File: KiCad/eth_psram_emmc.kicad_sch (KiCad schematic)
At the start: 42 parts, among them IC6 LAN8742A-CZ-TR, IC7 APS256XXN-OBR-BG, X2 5033981892, Y2 VXM7-9032-25M0000000

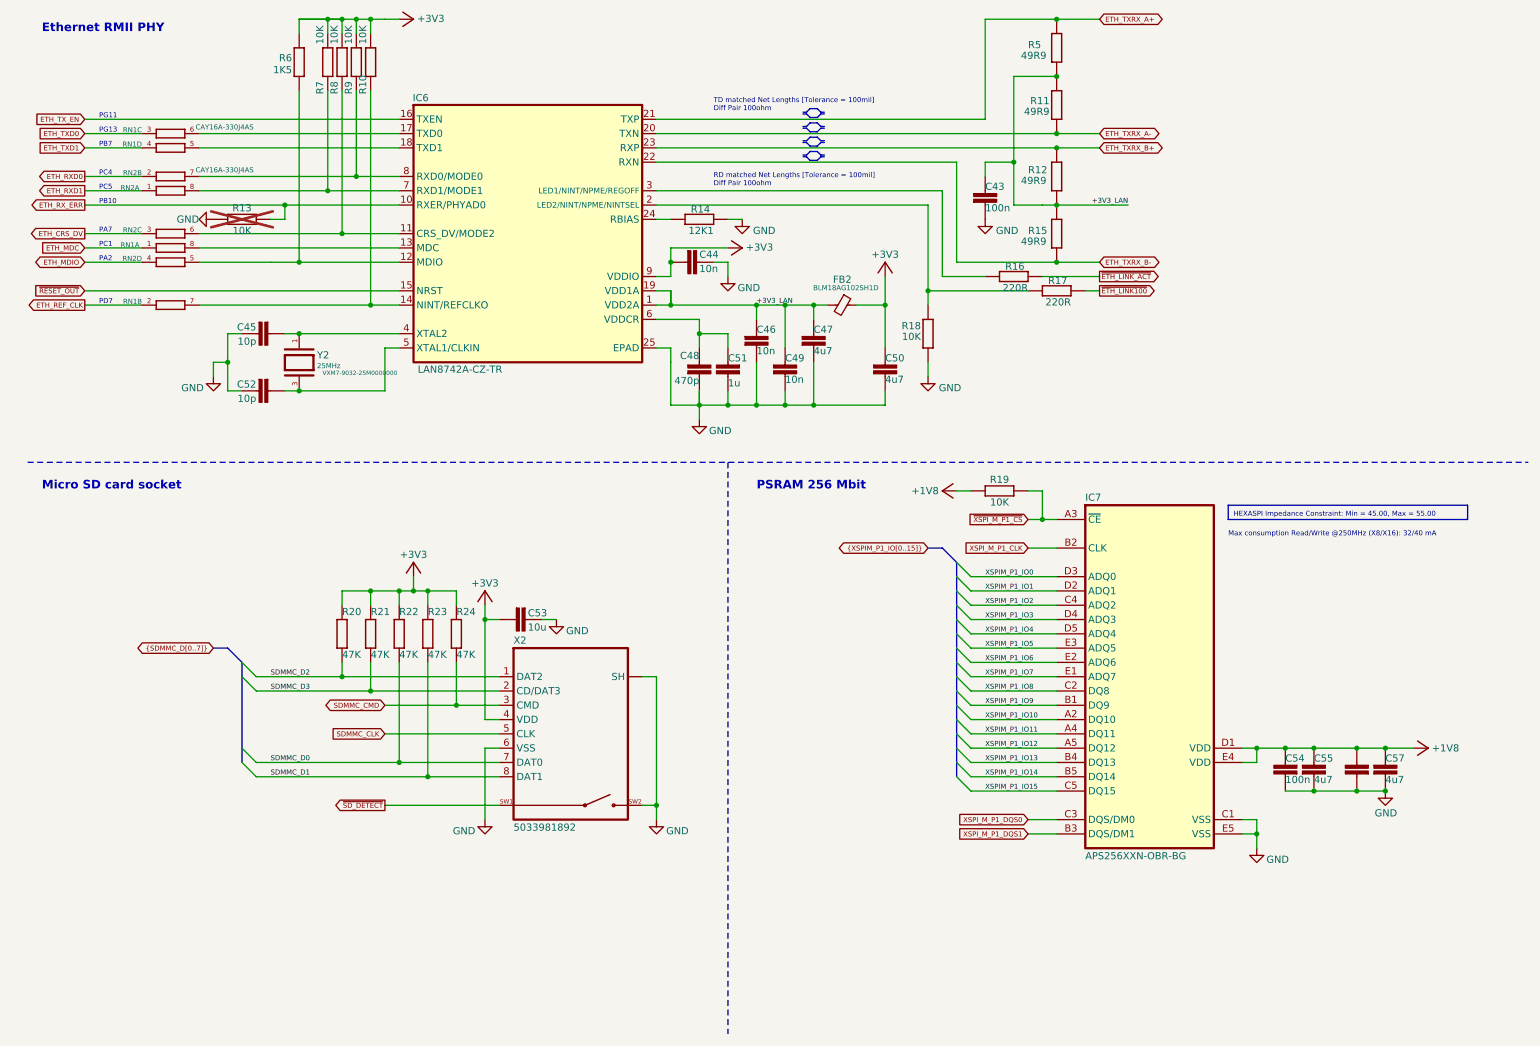
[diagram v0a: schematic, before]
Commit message: Split SoM footprint into two separate 100-pin connectors
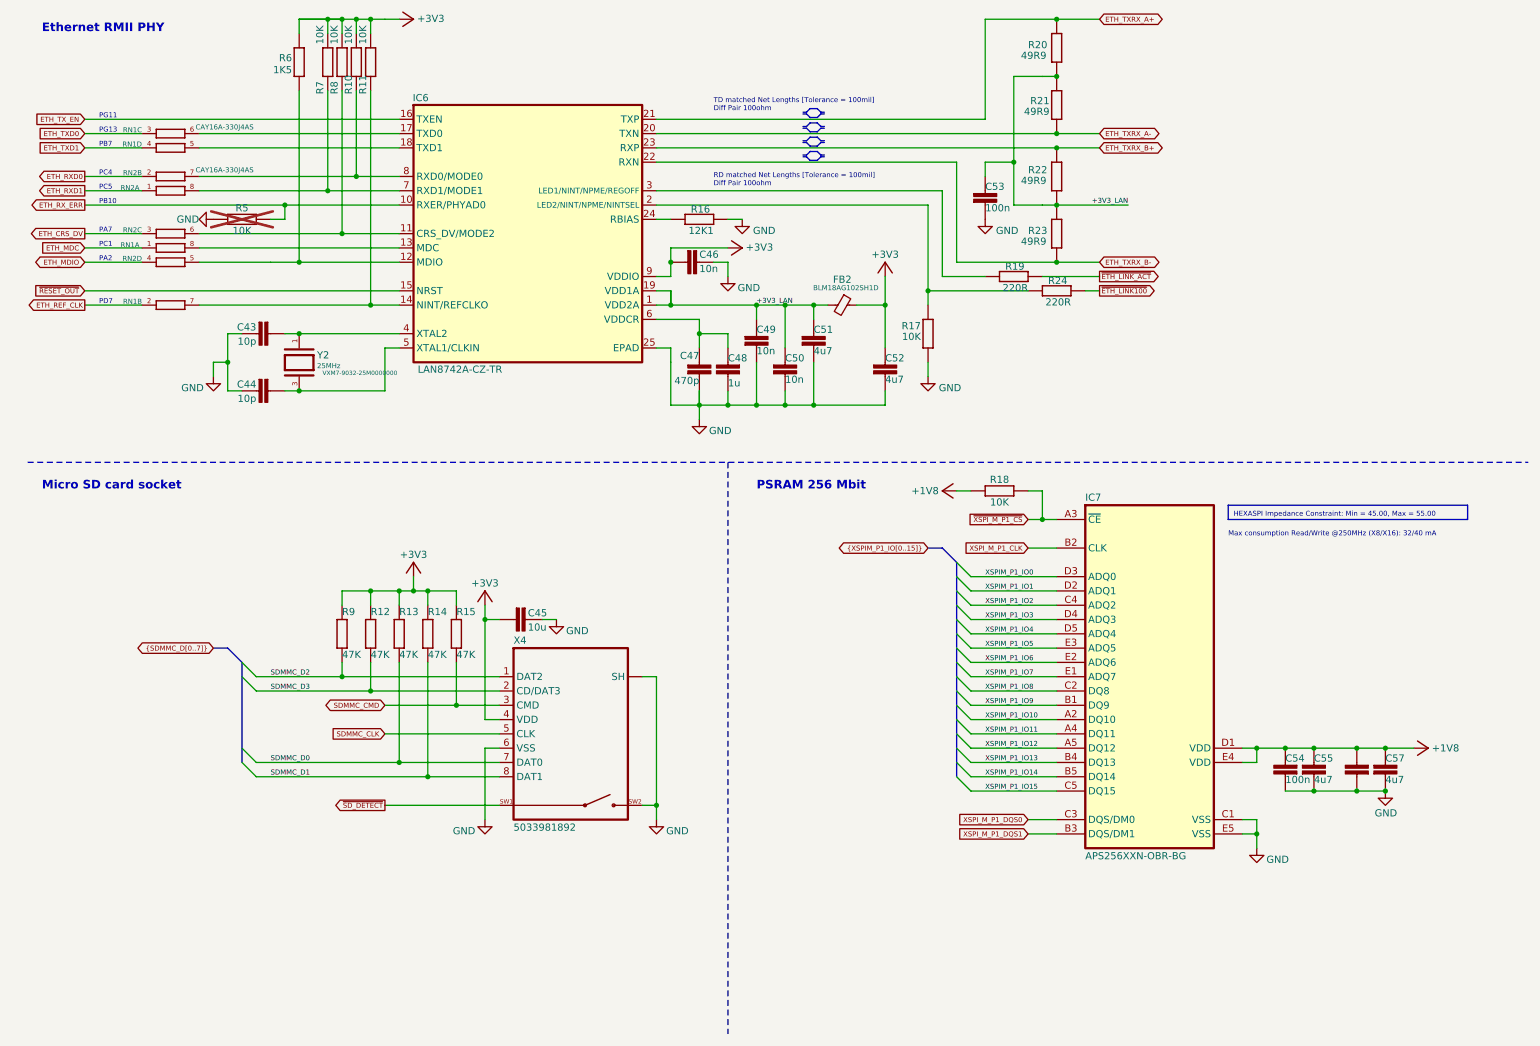
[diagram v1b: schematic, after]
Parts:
- renumbered C45 to C43, C52 to C44, C53 to C45, C44 to C46, C48 to C47, C51 to C48, C46 to C49, C49 to C50, C47 to C51, C50 to C52, C43 to C53, R9 to R10, R10 to R11, R21 to R12, R22 to R13, R23 to R14, R24 to R15, R14 to R16, R18 to R17, R19 to R18, R16 to R19, R5 to R20, R11 to R21, R12 to R22, R15 to R23, R17 to R24, R13 to R5, R20 to R9, X2 to X4

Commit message: #20
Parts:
- renumbered R9 to R10, R10 to R11, R11 to R12, R12 to R13, R13 to R14, R14 to R15, R15 to R16, R16 to R17, R17 to R18, R18 to R19, R19 to R20, R20 to R21, R21 to R22, R22 to R23, R23 to R24, R24 to R25, R5 to R6, R6 to R7, R7 to R8, R8 to R9
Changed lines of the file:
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@@
 	(title_block
 		(title "${project_name}")
-		(date "2026-04-18")
+		(date "2026-04-20")
 		(rev "${project_version}")
 		(company "${project_creator}")
@@
 		(in_pos_files yes)
 		(dnp no)
-		(property "Reference" "#+3V010"
+		(property "Reference" "#+3V011"
 			(at 83.82 15.24 0)
 			(hide yes)
@@
 			(project "BB3plus CM5 STM32H7 module"
 				(path "/1a4f0aea-3a69-423f-8790-3103cd0321c4/db533ab3-e8cc-4dba-934e-bd27ee1dfc29"
-					(reference "#+3V010")
+					(reference "#+3V011")
 					(unit 1)
 				)
@@
 		(in_pos_files yes)
 		(dnp no)
-		(property "Reference" "R16"
+		(property "Reference" "R17"
 			(at 136.525 48.26 90)
 			(show_name no)
@@
 			(project "BB3plus CM5 STM32H7 module"
 				(path "/1a4f0aea-3a69-423f-8790-3103cd0321c4/db533ab3-e8cc-4dba-934e-bd27ee1dfc29"
-					(reference "R16")
+					(reference "R17")
 					(unit 1)
 				)
@@
 		(in_pos_files yes)
 		(dnp no)
-		(property "Reference" "R7"
+		(property "Reference" "R8"
 			(at 67.945 28.575 90)
 			(show_name no)
@@
 			(project "BB3plus CM5 STM32H7 module"
 				(path "/1a4f0aea-3a69-423f-8790-3103cd0321c4/db533ab3-e8cc-4dba-934e-bd27ee1dfc29"
-					(reference "R7")
+					(reference "R8")
 					(unit 1)
 				)
@@
 		(in_pos_files yes)
 		(dnp no)
-		(property "Reference" "R14"
+		(property "Reference" "R15"
 			(at 86.36 121.285 0)
 			(show_name no)
@@
 			(project "BB3plus CM5 STM32H7 module"
 				(path "/1a4f0aea-3a69-423f-8790-3103cd0321c4/db533ab3-e8cc-4dba-934e-bd27ee1dfc29"
-					(reference "R14")
+					(reference "R15")
 					(unit 1)
 				)
@@
 		(in_pos_files yes)
 		(dnp no)
-		(property "Reference" "R9"
+		(property "Reference" "R10"
 			(at 71.12 121.285 0)
 			(show_name no)
@@
 			(project "BB3plus CM5 STM32H7 module"
 				(path "/1a4f0aea-3a69-423f-8790-3103cd0321c4/db533ab3-e8cc-4dba-934e-bd27ee1dfc29"
-					(reference "R9")
+					(reference "R10")
 					(unit 1)
 				)
@@
 		(in_pos_files yes)
 		(dnp no)
-		(property "Reference" "R20"
+		(property "Reference" "R21"
 			(at 193.04 19.05 0)
 			(show_name no)
@@
 			(project "BB3plus CM5 STM32H7 module"
 				(path "/1a4f0aea-3a69-423f-8790-3103cd0321c4/db533ab3-e8cc-4dba-934e-bd27ee1dfc29"
-					(reference "R20")
+					(reference "R21")
 					(unit 1)
 				)
@@
 		(in_pos_files yes)
 		(dnp no)
-		(property "Reference" "#PWR018"
+		(property "Reference" "#PWR019"
 			(at 260.35 144.78 0)
 			(hide yes)
@@
 			(project "BB3plus CM5 STM32H7 module"
 				(path "/1a4f0aea-3a69-423f-8790-3103cd0321c4/db533ab3-e8cc-4dba-934e-bd27ee1dfc29"
-					(reference "#PWR018")
+					(reference "#PWR019")
 					(unit 1)
 				)
@@
 		(in_pos_files yes)
 		(dnp no)
-		(property "Reference" "R12"
+		(property "Reference" "R13"
 			(at 76.2 121.285 0)
 			(show_name no)
@@
 			(project "BB3plus CM5 STM32H7 module"
 				(path "/1a4f0aea-3a69-423f-8790-3103cd0321c4/db533ab3-e8cc-4dba-934e-bd27ee1dfc29"
-					(reference "R12")
+					(reference "R13")
 					(unit 1)
 				)
@@
 		(in_pos_files yes)
 		(dnp no)
-		(property "Reference" "R8"
+		(property "Reference" "R9"
 			(at 70.485 28.575 90)
 			(show_name no)
@@
 			(project "BB3plus CM5 STM32H7 module"
 				(path "/1a4f0aea-3a69-423f-8790-3103cd0321c4/db533ab3-e8cc-4dba-934e-bd27ee1dfc29"
-					(reference "R8")
+					(reference "R9")
 					(unit 1)
 				)
@@
 		(in_pos_files yes)
 		(dnp no)
-		(property "Reference" "#PWR017"
+		(property "Reference" "#PWR018"
 			(at 181.61 99.06 0)
 			(hide yes)
@@
 			(project "BB3plus CM5 STM32H7 module"
 				(path "/1a4f0aea-3a69-423f-8790-3103cd0321c4/db533ab3-e8cc-4dba-934e-bd27ee1dfc29"
-					(reference "#PWR017")
+					(reference "#PWR018")
 					(unit 1)
 				)
@@
 		(in_pos_files yes)
 		(dnp no)
-		(property "Reference" "R23"
+		(property "Reference" "R24"
 			(at 193.04 52.07 0)
 			(show_name no)
@@
 			(project "BB3plus CM5 STM32H7 module"
 				(path "/1a4f0aea-3a69-423f-8790-3103cd0321c4/db533ab3-e8cc-4dba-934e-bd27ee1dfc29"
-					(reference "R23")
+					(reference "R24")
 					(unit 1)
 				)
@@
 		(in_pos_files yes)
 		(dnp no)
-		(property "Reference" "R17"
+		(property "Reference" "R18"
 			(at 173.99 70.485 0)
 			(show_name no)
@@
 			(project "BB3plus CM5 STM32H7 module"
 				(path "/1a4f0aea-3a69-423f-8790-3103cd0321c4/db533ab3-e8cc-4dba-934e-bd27ee1dfc29"
-					(reference "R17")
+					(reference "R18")
 					(unit 1)
 				)
@@
 		(in_pos_files yes)
 		(dnp no)
-		(property "Reference" "#+3V013"
+		(property "Reference" "#+3V014"
 			(at 142.24 55.88 0)
 			(hide yes)
@@
 			(project "BB3plus CM5 STM32H7 module"
 				(path "/1a4f0aea-3a69-423f-8790-3103cd0321c4/db533ab3-e8cc-4dba-934e-bd27ee1dfc29"
-					(reference "#+3V013")
+					(reference "#+3V014")
 					(unit 1)
 				)
@@
 		(in_pos_files yes)
 		(dnp no)
-		(property "Reference" "R19"
+		(property "Reference" "R20"
 			(at 192.405 58.42 90)
 			(show_name no)
@@
 			(project "BB3plus CM5 STM32H7 module"
 				(path "/1a4f0aea-3a69-423f-8790-3103cd0321c4/db533ab3-e8cc-4dba-934e-bd27ee1dfc29"
-					(reference "R19")
+					(reference "R20")
 					(unit 1)
 				)
@@
 		(in_pos_files yes)
 		(dnp no)
-		(property "Reference" "R13"
+		(property "Reference" "R14"
 			(at 81.28 121.285 0)
 			(show_name no)
@@
 			(project "BB3plus CM5 STM32H7 module"
 				(path "/1a4f0aea-3a69-423f-8790-3103cd0321c4/db533ab3-e8cc-4dba-934e-bd27ee1dfc29"
-					(reference "R13")
+					(reference "R14")
 					(unit 1)
 				)
@@
 		(in_pos_files yes)
 		(dnp no)
-		(property "Reference" "R6"
+		(property "Reference" "R7"
 			(at 62.23 22.86 0)
 			(show_name no)
@@
 			(project "BB3plus CM5 STM32H7 module"
 				(path "/1a4f0aea-3a69-423f-8790-3103cd0321c4/db533ab3-e8cc-4dba-934e-bd27ee1dfc29"
-					(reference "R6")
+					(reference "R7")
 					(unit 1)
 				)
@@
 		(in_pos_files yes)
 		(dnp no)
-		(property "Reference" "R15"
+		(property "Reference" "R16"
 			(at 91.44 121.285 0)
 			(show_name no)
@@
 			(project "BB3plus CM5 STM32H7 module"
 				(path "/1a4f0aea-3a69-423f-8790-3103cd0321c4/db533ab3-e8cc-4dba-934e-bd27ee1dfc29"
-					(reference "R15")
+					(reference "R16")
 					(unit 1)
 				)
@@
 		(in_pos_files yes)
 		(dnp yes)
-		(property "Reference" "R5"
+		(property "Reference" "R6"
 			(at 53.34 49.53 90)
 			(show_name no)
@@
 			(project "BB3plus CM5 STM32H7 module"
 				(path "/1a4f0aea-3a69-423f-8790-3103cd0321c4/db533ab3-e8cc-4dba-934e-bd27ee1dfc29"
-					(reference "R5")
+					(reference "R6")
 					(unit 1)
 				)
@@
 		(in_pos_files yes)
 		(dnp no)
-		(property "Reference" "R21"
+		(property "Reference" "R22"
 			(at 196.85 30.48 0)
 			(show_name no)
@@
 			(project "BB3plus CM5 STM32H7 module"
 				(path "/1a4f0aea-3a69-423f-8790-3103cd0321c4/db533ab3-e8cc-4dba-934e-bd27ee1dfc29"
-					(reference "R21")
+					(reference "R22")
 					(unit 1)
 				)
@@
 		(in_pos_files yes)
 		(dnp no)
-		(property "Reference" "R18"
+		(property "Reference" "R19"
 			(at 187.96 97.79 90)
 			(show_name no)
@@
 			(project "BB3plus CM5 STM32H7 module"
 				(path "/1a4f0aea-3a69-423f-8790-3103cd0321c4/db533ab3-e8cc-4dba-934e-bd27ee1dfc29"
-					(reference "R18")
+					(reference "R19")
 					(unit 1)
 				)
@@
 		(in_pos_files yes)
 		(dnp no)
-		(property "Reference" "R22"
+		(property "Reference" "R23"
 			(at 193.04 41.275 0)
 			(show_name no)
@@
 			(project "BB3plus CM5 STM32H7 module"
 				(path "/1a4f0aea-3a69-423f-8790-3103cd0321c4/db533ab3-e8cc-4dba-934e-bd27ee1dfc29"
-					(reference "R22")
+					(reference "R23")
 					(unit 1)
 				)
@@
 		(in_pos_files yes)
 		(dnp no)
-		(property "Reference" "#+3V012"
+		(property "Reference" "#+3V013"
 			(at 96.52 116.84 0)
 			(hide yes)
@@
 			(project "BB3plus CM5 STM32H7 module"
 				(path "/1a4f0aea-3a69-423f-8790-3103cd0321c4/db533ab3-e8cc-4dba-934e-bd27ee1dfc29"
-					(reference "#+3V012")
+					(reference "#+3V013")
 					(unit 1)
 				)
@@
 		(in_pos_files yes)
 		(dnp no)
-		(property "Reference" "R24"
+		(property "Reference" "R25"
 			(at 200.025 60.96 90)
 			(show_name no)
@@
 			(project "BB3plus CM5 STM32H7 module"
 				(path "/1a4f0aea-3a69-423f-8790-3103cd0321c4/db533ab3-e8cc-4dba-934e-bd27ee1dfc29"
-					(reference "R24")
+					(reference "R25")
 					(unit 1)
 				)
@@
 		(in_pos_files yes)
 		(dnp no)
-		(property "Reference" "#+3V014"
+		(property "Reference" "#+3V015"
 			(at 167.64 58.42 0)
 			(hide yes)
@@
 			(project "BB3plus CM5 STM32H7 module"
 				(path "/1a4f0aea-3a69-423f-8790-3103cd0321c4/db533ab3-e8cc-4dba-934e-bd27ee1dfc29"
-					(reference "#+3V014")
+					(reference "#+3V015")
 					(unit 1)
 				)
@@
 		(in_pos_files yes)
 		(dnp no)
-		(property "Reference" "#+3V011"
+		(property "Reference" "#+3V012"
 			(at 83.82 111.76 0)
 			(hide yes)
@@
 			(project "BB3plus CM5 STM32H7 module"
 				(path "/1a4f0aea-3a69-423f-8790-3103cd0321c4/db533ab3-e8cc-4dba-934e-bd27ee1dfc29"
-					(reference "#+3V011")
+					(reference "#+3V012")
 					(unit 1)
 				)
@@
 		(in_pos_files yes)
 		(dnp no)
-		(property "Reference" "R10"
+		(property "Reference" "R11"
 			(at 73.025 28.575 90)
 			(show_name no)
@@
 			(project "BB3plus CM5 STM32H7 module"
 				(path "/1a4f0aea-3a69-423f-8790-3103cd0321c4/db533ab3-e8cc-4dba-934e-bd27ee1dfc29"
-					(reference "R10")
+					(reference "R11")
 					(unit 1)
 				)
@@
 		(in_pos_files yes)
 		(dnp no)
-		(property "Reference" "R11"
+		(property "Reference" "R12"
 			(at 75.565 28.575 90)
 			(show_name no)
@@
 			(project "BB3plus CM5 STM32H7 module"
 				(path "/1a4f0aea-3a69-423f-8790-3103cd0321c4/db533ab3-e8cc-4dba-934e-bd27ee1dfc29"
-					(reference "R11")
+					(reference "R12")
 					(unit 1)
 				)

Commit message: #21
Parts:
- added JP2: (no value), PCM_EEZ_SMD:JP3 shorted (0603), symbol PCM_EEZ_unsorted:JP3 shorted
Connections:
- net ~{RESET_OUT}: now also JP2.NC; no longer IC6.15 (NRST)
- new net: IC6.15 (NRST), JP2.COM
- new net ~{ETH_RESET}: JP2.NO
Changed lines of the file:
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@@
 	)
 	(junction
-		(at 71.12 53.34)
+		(at 76.2 66.04)
 		(diameter 0)
 		(color 0 0 0 0)
 	)
 	(junction
-		(at 233.68 160.02)
+		(at 71.12 53.34)
 		(diameter 0)
 		(color 0 0 0 0)
 	)
 	(junction
-		(at 144.78 83.82)
+		(at 233.68 160.02)
 		(diameter 0)
 		(color 0 0 0 0)
 	)
 	(junction
-		(at 134.62 83.82)
+		(at 144.78 83.82)
 		(diameter 0)
 		(color 0 0 0 0)
 	)
 	(junction
-		(at 76.2 66.04)
+		(at 134.62 83.82)
 		(diameter 0)
 		(color 0 0 0 0)
@@
 	(wire
 		(pts
+			(xy 38.1 76.2) (xy 38.1 78.74)
+		)
+		(stroke
+			(width 0)
+			(type default)
+		)
+	)
+	(wire
+		(pts
 			(xy 71.12 129.54) (xy 71.12 132.08)
 		)
@@
 	(wire
 		(pts
+			(xy 40.64 73.66) (xy 48.26 73.66)
+		)
+		(stroke
+			(width 0)
+			(type default)
+		)
+	)
+	(wire
+		(pts
 			(xy 182.88 137.16) (xy 198.12 137.16)
 		)
@@
 	(wire
 		(pts
+			(xy 25.4 78.74) (xy 38.1 78.74)
+		)
+		(stroke
+			(width 0)
+			(type default)
+		)
+	)
+	(wire
+		(pts
 			(xy 134.62 86.36) (xy 134.62 83.82)
 		)
@@
 	(wire
 		(pts
+			(xy 48.26 63.5) (xy 81.28 63.5)
+		)
+		(stroke
+			(width 0.1524)
+			(type solid)
+		)
+	)
+	(wire
+		(pts
 			(xy 60.96 81.28) (xy 63.5 81.28)
 		)
@@
 	(wire
 		(pts
+			(xy 25.4 68.58) (xy 38.1 68.58)
+		)
+		(stroke
+			(width 0)
+			(type default)
+		)
+	)
+	(wire
+		(pts
 			(xy 76.2 15.24) (xy 76.2 17.78)
 		)
@@
 	(wire
 		(pts
+			(xy 25.4 66.04) (xy 35.56 66.04)
+		)
+		(stroke
+			(width 0)
+			(type default)
+		)
+	)
+	(wire
+		(pts
 			(xy 129.54 60.96) (xy 127 60.96)
 		)
@@
 	(wire
 		(pts
+			(xy 38.1 68.58) (xy 38.1 71.12)
+		)
+		(stroke
+			(width 0)
+			(type default)
+		)
+	)
+	(wire
+		(pts
 			(xy 25.4 55.88) (xy 35.56 55.88)
 		)
@@
 	(wire
 		(pts
+			(xy 48.26 63.5) (xy 48.26 73.66)
+		)
+		(stroke
+			(width 0)
+			(type default)
+		)
+	)
+	(wire
+		(pts
 			(xy 182.88 139.7) (xy 198.12 139.7)
 		)
@@
 	(wire
 		(pts
-			(xy 25.4 66.04) (xy 35.56 66.04)
-		)
-		(stroke
-			(width 0)
-			(type default)
-		)
-	)
-	(wire
-		(pts
 			(xy 76.2 116.84) (xy 81.28 116.84)
 		)
@@
 		)
 	)
-	(wire
-		(pts
-			(xy 25.4 63.5) (xy 81.28 63.5)
-		)
-		(stroke
-			(width 0.1524)
-			(type solid)
-		)
-	)
 	(polyline
 		(pts
@@
 	(global_label "~{RESET_OUT}"
 		(shape input)
-		(at 25.4 63.5 180)
+		(at 25.4 78.74 180)
 		(fields_autoplaced yes)
 		(effects
@@
 		)
 		(property "Intersheetrefs" "${INTERSHEET_REFS}"
-			(at 16.5296 63.5 0)
+			(at 16.5296 78.74 0)
 			(hide yes)
 			(show_name no)
@@
 		)
 	)
+	(global_label "~{ETH_RESET}"
+		(shape input)
+		(at 25.4 68.58 180)
+		(fields_autoplaced yes)
+		(effects
+			(font
+				(size 0.889 0.889)
+				(color 204 102 0 1)
+			)
+			(justify right)
+		)
+		(property "Intersheetrefs" "${INTERSHEET_REFS}"
+			(at 16.6566 68.58 0)
+			(hide yes)
+			(show_name no)
+			(do_not_autoplace no)
+			(effects
+				(font
+					(size 1.27 1.27)
+				)
+				(justify right)
+			)
+		)
+	)
 	(global_label "ETH_REF_CLK"
 		(shape output)
@@
 		(dnp no)
 		(property "Reference" "R8"
-			(at 67.945 28.575 90)
+			(at 67.945 26.035 90)
 			(show_name no)
 			(do_not_autoplace no)
@@
 					(size 1.27 1.27)
 				)
-				(justify right top)
+				(justify left top)
 			)
 		)
@@
 	)
 	(symbol
+		(lib_id "PCM_EEZ_unsorted:JP3 shorted")
+		(at 38.1 73.66 0)
+		(unit 1)
+		(body_style 1)
+		(exclude_from_sim no)
+		(in_bom no)
+		(on_board yes)
+		(in_pos_files yes)
+		(dnp no)
+		(property "Reference" "JP2"
+			(at 36.83 73.6599 0)
+			(show_name no)
+			(do_not_autoplace no)
+			(effects
+				(font
+					(size 1.27 1.27)
+				)
+				(justify right)
+			)
+		)
+		(property "Value" ""
+			(at 38.1 73.66 90)
+			(hide yes)
+			(show_name no)
+			(do_not_autoplace no)
+			(effects
+				(font
+					(size 1.27 1.27)
+				)
+			)
+		)
+		(property "Footprint" "PCM_EEZ_SMD:JP3 shorted (0603)"
+			(at 38.1 78.74 0)
+			(hide yes)
+			(show_name no)
+			(do_not_autoplace no)
+			(effects
+				(font
+					(size 1.27 1.27)
+				)
+			)
+		)
+		(property "Datasheet" ""
+			(at 38.1 73.66 0)
+			(hide yes)
+			(show_name no)
+			(do_not_autoplace no)
+			(effects
+				(font
+					(size 1.27 1.27)
+				)
+			)
+		)
+		(property "Description" ""
+			(at 38.1 73.66 0)
+			(hide yes)
+			(show_name no)
+			(do_not_autoplace no)
+			(effects
+				(font
+					(size 1.27 1.27)
+				)
+			)
+		)
+		(property "Type" ""
+			(at 38.1 73.66 90)
+			(hide yes)
+			(show_name no)
+			(do_not_autoplace no)
+			(effects
+				(font
+					(size 1.27 1.27)
+				)
+			)
+		)
+		(property "DigiKey" ""
+			(at 38.1 73.66 0)
+			(hide yes)
+			(show_name no)
+			(do_not_autoplace no)
+			(effects
+				(font
+					(size 1.27 1.27)
+				)
+			)
+		)
+		(property "Mouser" ""
+			(at 38.1 73.66 0)
+			(hide yes)
+			(show_name no)
+			(do_not_autoplace no)
+			(effects
+				(font
+					(size 1.27 1.27)
+				)
+			)
+		)
+		(property "TME" ""
+			(at 38.1 73.66 0)
+			(hide yes)
+			(show_name no)
+			(do_not_autoplace no)
+			(effects
+				(font
+					(size 1.27 1.27)
+				)
+			)
+		)
+		(property "LCSC" ""
+			(at 38.1 73.66 0)
+			(hide yes)
+			(show_name no)
+			(do_not_autoplace no)
+			(effects
+				(font
+					(size 1.27 1.27)
+				)
+			)
+		)
+		(pin "COM"
+		)
+		(pin "NC"
+		)
+		(pin "NO"
+		)
+		(instances
+			(project "BB3plus CM5 STM32H7 module"
+				(path "/1a4f0aea-3a69-423f-8790-3103cd0321c4/db533ab3-e8cc-4dba-934e-bd27ee1dfc29"
+					(reference "JP2")
+					(unit 1)
+				)
+			)
+		)
+	)
+	(symbol
 		(lib_id "PCM_EEZ_passives:C-EU")
 		(at 238.76 147.32 0)
@@
 		(dnp no)
 		(property "Reference" "R9"
-			(at 70.485 28.575 90)
+			(at 70.485 26.035 90)
 			(show_name no)
 			(do_not_autoplace no)
@@
 					(size 1.27 1.27)
 				)
-				(justify left bottom)
+				(justify right bottom)
 			)
 		)
@@
 		(dnp no)
 		(property "Reference" "R11"
-			(at 73.025 28.575 90)
+			(at 73.025 26.035 90)
 			(show_name no)
 			(do_not_autoplace no)
@@
 					(size 1.27 1.27)
 				)
-				(justify left bottom)
+				(justify right bottom)
 			)
 		)
@@
 		(dnp no)
 		(property "Reference" "R12"
-			(at 75.565 28.575 90)
+			(at 75.565 26.035 90)
 			(show_name no)
 			(do_not_autoplace no)
@@
 					(size 1.27 1.27)
 				)
-				(justify left bottom)
+				(justify right bottom)
 			)
 		)
